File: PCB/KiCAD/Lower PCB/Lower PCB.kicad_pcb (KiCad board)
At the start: 2 copper layers, 179.5 x 163.2 mm, 0 parts

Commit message: Start of PCBs
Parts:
- added C1: 100nF, Capacitor_SMD:C_0805_2012Metric_Pad1.18x1.45mm_HandSolder, F.Cu at (-2.28, 6.00)
- added C10: 10nF, Capacitor_SMD:C_1210_3225Metric_Pad1.33x2.70mm_HandSolder, F.Cu at (-56.5, 25.0)
- added C11: 10nF, Capacitor_SMD:C_1210_3225Metric_Pad1.33x2.70mm_HandSolder, F.Cu at (-56.6, 30.5)
- added C12: 0.1uF, Capacitor_SMD:C_0805_2012Metric_Pad1.18x1.45mm_HandSolder, F.Cu at (-51.0, 31.5)
- added C13: 10nF, Capacitor_SMD:C_1210_3225Metric_Pad1.33x2.70mm_HandSolder, F.Cu at (-57.5, -30.5)
- added C14: 10nF, Capacitor_SMD:C_1210_3225Metric_Pad1.33x2.70mm_HandSolder, F.Cu at (-57.5, -24.5)
- added C15: 0.1uF, Capacitor_SMD:C_0805_2012Metric_Pad1.18x1.45mm_HandSolder, F.Cu at (-52.0, -24.0)
- added C16: 220uF, Capacitor_SMD:CP_Elec_10x10, F.Cu at (43.5, -13.0)
- added C17: 220uF, Capacitor_SMD:CP_Elec_10x10, F.Cu at (43.0, 12.5)
- added C18: 0.1uF, Capacitor_SMD:C_0805_2012Metric_Pad1.18x1.45mm_HandSolder, F.Cu at (53.0, -27.5)
- added C19: 0.1uF, Capacitor_SMD:C_0805_2012Metric_Pad1.18x1.45mm_HandSolder, F.Cu at (53.5, 27.0)
- added C2: 100nF, Capacitor_SMD:C_0805_2012Metric_Pad1.18x1.45mm_HandSolder, F.Cu at (-2.28, 9.01)
- added C20: 10nF, Capacitor_SMD:C_1210_3225Metric_Pad1.33x2.70mm_HandSolder, F.Cu at (47.5, -30.5)
- added C21: 100nF, Capacitor_SMD:C_0805_2012Metric_Pad1.18x1.45mm_HandSolder, F.Cu at (20.5, -30.0)
- added C22: 100nF, Capacitor_SMD:C_0805_2012Metric_Pad1.18x1.45mm_HandSolder, F.Cu at (20.6, -26.5)
- added C23: 22pF, Capacitor_SMD:C_0805_2012Metric_Pad1.18x1.45mm_HandSolder, F.Cu at (26.1, -30.0)
- added C24: 22pF, Capacitor_SMD:C_0805_2012Metric_Pad1.18x1.45mm_HandSolder, F.Cu at (26.1, -26.5)
- added C25: 100nF, Capacitor_SMD:C_0805_2012Metric_Pad1.18x1.45mm_HandSolder, F.Cu at (20.6, -23.0)
- added C26: 10nF, Capacitor_SMD:C_1210_3225Metric_Pad1.33x2.70mm_HandSolder, F.Cu at (47.5, -24.5)
- added C27: 0.1uF, Capacitor_SMD:C_0805_2012Metric_Pad1.18x1.45mm_HandSolder, F.Cu at (53.0, -24.0)
- added C28: 10nF, Capacitor_SMD:C_1210_3225Metric_Pad1.33x2.70mm_HandSolder, F.Cu at (48.0, 24.0)
- added C29: 10nF, Capacitor_SMD:C_1210_3225Metric_Pad1.33x2.70mm_HandSolder, F.Cu at (48.0, 30.0)
- added C3: 100nF, Capacitor_SMD:C_0805_2012Metric_Pad1.18x1.45mm_HandSolder, F.Cu at (-2.28, 12.0)
- added C30: 0.1uF, Capacitor_SMD:C_0805_2012Metric_Pad1.18x1.45mm_HandSolder, F.Cu at (53.5, 30.5)
- added C4: 22pF, Capacitor_SMD:C_0805_2012Metric_Pad1.18x1.45mm_HandSolder, F.Cu at (-2.28, 15.0)
- added C5: 22pF, Capacitor_SMD:C_0805_2012Metric_Pad1.18x1.45mm_HandSolder, F.Cu at (-2.28, 18.0)
- added C6: 220uF, Capacitor_SMD:CP_Elec_10x10, F.Cu at (-42.5, 12.5)
- added C7: 220uF, Capacitor_SMD:CP_Elec_10x10, F.Cu at (-42.0, -12.0)
- added C8: 0.1uF, Capacitor_SMD:C_0805_2012Metric_Pad1.18x1.45mm_HandSolder, F.Cu at (-51.0, 28.0)
- added C9: 0.1uF, Capacitor_SMD:C_0805_2012Metric_Pad1.18x1.45mm_HandSolder, F.Cu at (-52.0, -27.5)
- added D1: RED_LED, LED_SMD:LED_0805_2012Metric_Pad1.15x1.40mm_HandSolder, F.Cu at (2.54, 6.01)
- added D2: GREEN_LED, LED_SMD:LED_0805_2012Metric_Pad1.15x1.40mm_HandSolder, F.Cu at (2.54, 9.05)
- added D3: RED_LED, LED_SMD:LED_0805_2012Metric_Pad1.15x1.40mm_HandSolder, F.Cu at (31.0, -23.5)
- added D4: GREEN_LED, LED_SMD:LED_0805_2012Metric_Pad1.15x1.40mm_HandSolder, F.Cu at (31.0, -20.5)
- added F1: Fuse, Fuse:Fuseholder_Blade_Mini_Keystone_3568, F.Cu at (-6.20, -56.0)
- added J2: Conn_01x02, Connector_AMASS:AMASS_XT60-M_1x02_P7.20mm_Vertical, F.Cu at (-13.5, -64.6)
- added M1: Conn_01x02_Pin, Connector_Molex:Molex_KK-254_AE-6410-02A_1x02_P2.54mm_Vertical, F.Cu at (-46.5, 27.0)
- added M2: Conn_01x02_Pin, Connector_Molex:Molex_KK-254_AE-6410-02A_1x02_P2.54mm_Vertical, F.Cu at (-47.5, -28.5)
- added M3: Conn_01x02_Pin, Connector_Molex:Molex_KK-254_AE-6410-02A_1x02_P2.54mm_Vertical, F.Cu at (57.5, -28.5)
- added M4: Conn_01x02_Pin, Connector_Molex:Molex_KK-254_AE-6410-02A_1x02_P2.54mm_Vertical, F.Cu at (58.0, 26.0)
- added R1: 2.7k, Resistor_SMD:R_0805_2012Metric_Pad1.20x1.40mm_HandSolder, F.Cu at (-51.1, 24.5)
- added R12: 2.7k, Resistor_SMD:R_0805_2012Metric_Pad1.20x1.40mm_HandSolder, F.Cu at (53.0, -31.0)
- added R13: 2.7k, Resistor_SMD:R_0805_2012Metric_Pad1.20x1.40mm_HandSolder, F.Cu at (53.5, 23.5)
- added R2: 330, Resistor_SMD:R_0805_2012Metric_Pad1.20x1.40mm_HandSolder, F.Cu at (2.50, 12.1)
- added R3: 330, Resistor_SMD:R_0805_2012Metric_Pad1.20x1.40mm_HandSolder, F.Cu at (2.50, 15.0)
- added R4: 330, Resistor_SMD:R_0805_2012Metric_Pad1.20x1.40mm_HandSolder, F.Cu at (2.69, 18.1)
- added R5: 2.7k, Resistor_SMD:R_0805_2012Metric_Pad1.20x1.40mm_HandSolder, F.Cu at (-52.0, -31.0)
- added R6: 330, Resistor_SMD:R_0805_2012Metric_Pad1.20x1.40mm_HandSolder, F.Cu at (14.6, -30.0)
- added R7: 330, Resistor_SMD:R_0805_2012Metric_Pad1.20x1.40mm_HandSolder, F.Cu at (14.6, -26.5)
- added S1: 1101M2S3CGE2, 1101M2S3CGE2:1101M2S3CGE2, F.Cu at (4.00, -64.7)
- added U1: ATmega328PB-A, Package_QFP:TQFP-32_7x7mm_P0.8mm, F.Cu at (-11.8, 12.2)
- added U2: LMD18200, Package_TO_SOT_THT:TO-220-11_P3.4x5.08mm_StaggerOdd_Lead4.58mm_Vertical, F.Cu at (-50.5, 8.42)
- added U3: LMD18200, Package_TO_SOT_THT:TO-220-11_P3.4x5.08mm_StaggerOdd_Lead4.58mm_Vertical, F.Cu at (-67.4, -7.92)
- added U4: LMD18200, Package_TO_SOT_THT:TO-220-11_P3.4x5.08mm_StaggerOdd_Lead4.58mm_Vertical, F.Cu at (51.7, -8.42)
- added U5: LMD18200, Package_TO_SOT_THT:TO-220-11_P3.4x5.08mm_StaggerOdd_Lead4.58mm_Vertical, F.Cu at (68.5, 8.42)
- added U6: ATmega328PB-A, Package_QFP:TQFP-32_7x7mm_P0.8mm, F.Cu at (7.50, -8.50)
- added U7: ~, Pololu:D36V28F5, F.Cu at (0.00, -42.5)
- added Y1: Crystal, Crystal:Crystal_SMD_3225-4Pin_3.2x2.5mm_HandSoldering, F.Cu at (-13.0, 1.00)
- added Y2: Crystal, Crystal:Crystal_SMD_3225-4Pin_3.2x2.5mm_HandSoldering, F.Cu at (32.1, -28.6)
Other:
- outline, holes or cut-outs redrawn

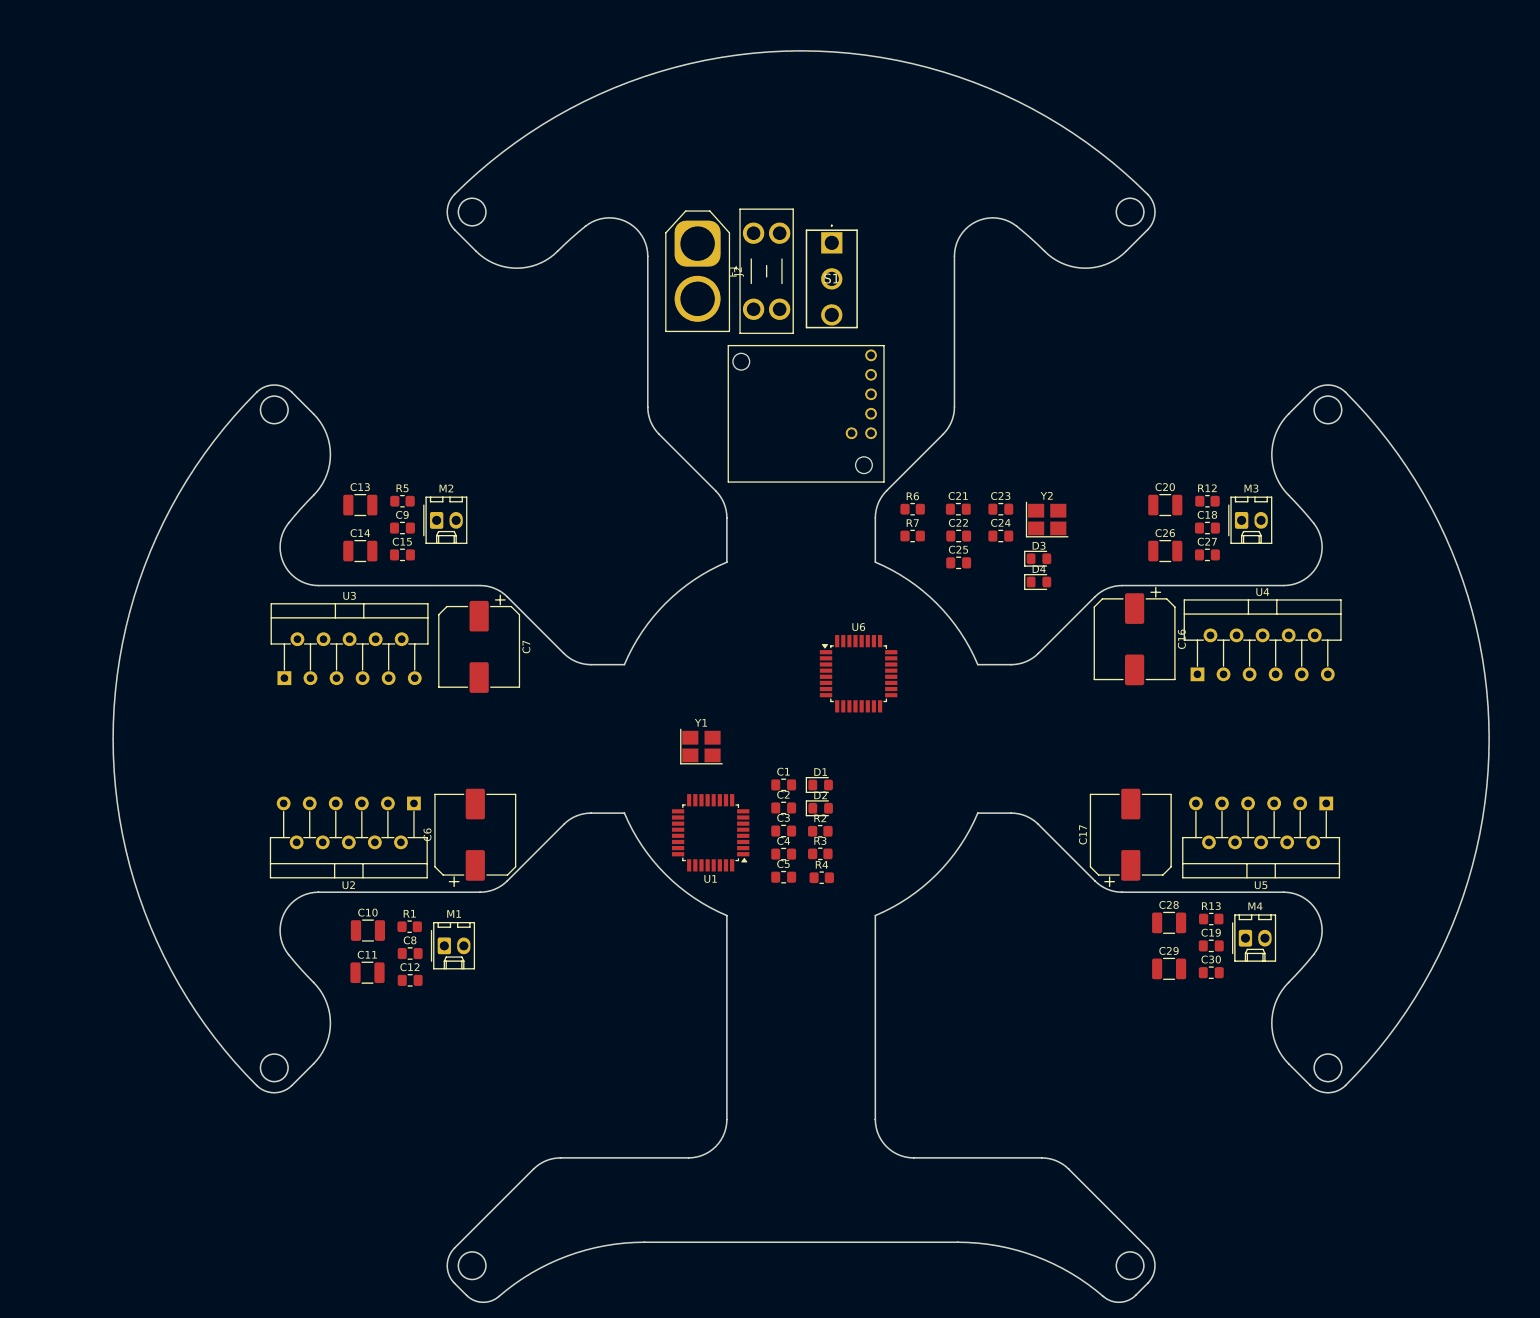
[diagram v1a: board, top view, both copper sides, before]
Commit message: Placed components on Lower PCB
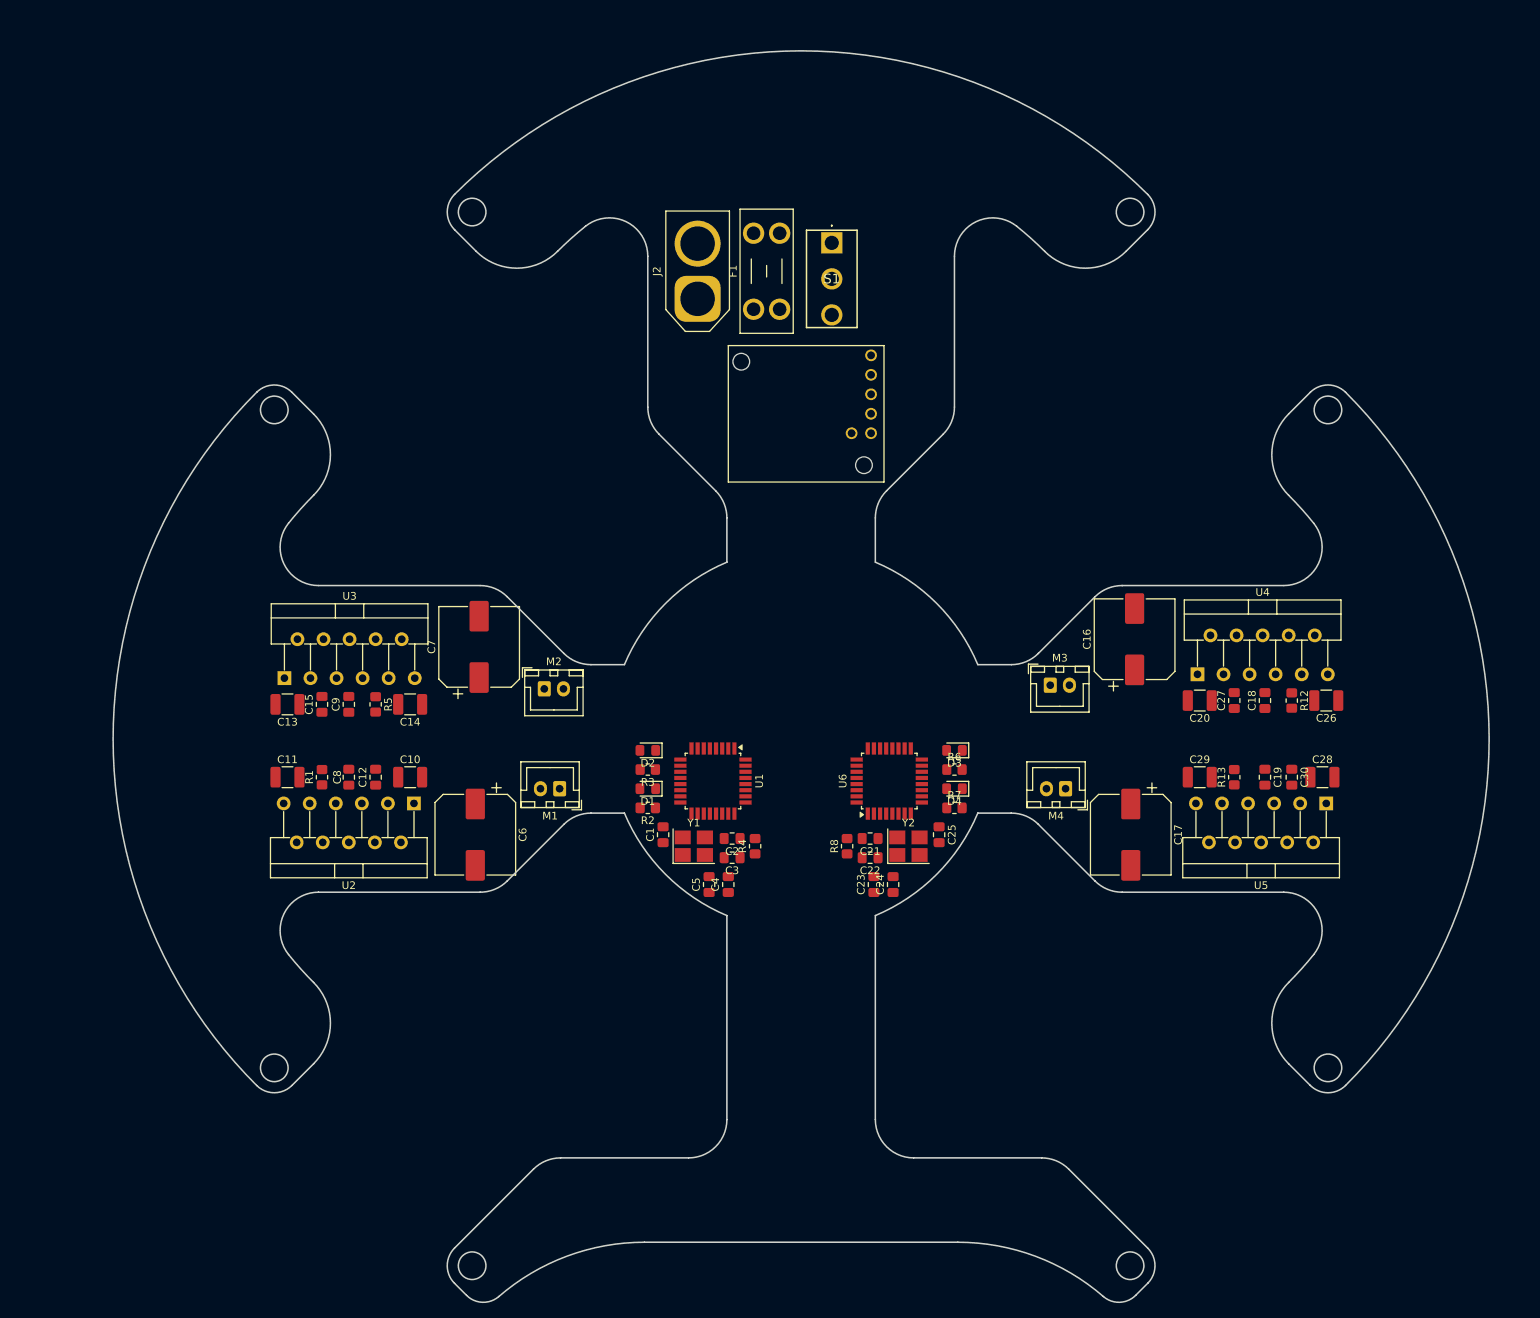
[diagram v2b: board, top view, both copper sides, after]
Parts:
- added R8: 10k, Resistor_SMD:R_0805_2012Metric_Pad1.20x1.40mm_HandSolder, F.Cu at (6.00, 14.0)
- M1, M2, M3, M4: footprint Connector_Molex:Molex_KK-254_AE-6410-02A_1x02_P2.54mm_Vertical -> Connector_JST:JST_XH_B2B-XH-A_1x02_P2.50mm_Vertical
- R4: value 330 -> 10k
- moved C23 51.7 mm to (9.50, 19.0), turned to 90 degrees
- moved C24 47.6 mm to (12.0, 19.0), turned to 90 degrees
- moved Y2 46.3 mm to (14.0, 14.0)
- moved C21 44.5 mm to (9.00, 13.0), turned to 180 degrees
- moved C22 43.5 mm to (9.00, 15.5), turned to 180 degrees
- moved R7 35.9 mm to (20.0, 9.00)
- moved C25 35.6 mm to (18.0, 12.5), turned to -90 degrees
- moved R6 34.4 mm to (20.0, 4.00)
- moved M3 32.9 mm to (32.5, -7.00)
- moved M4 30.5 mm to (34.5, 6.50), turned to 180 degrees
- moved D4 29.1 mm to (20.0, 6.50), turned to 180 degrees
- moved C26 28.7 mm to (68.5, -5.00), turned to 180 degrees
- moved R12 28.2 mm to (64.0, -5.00), turned to -90 degrees
- moved C13 27.7 mm to (-67.0, -4.50), turned to 180 degrees
- moved C28 27.6 mm to (68.0, 5.00)
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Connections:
- U6 pad 29: unconnected-(U6-~{RESET}/PC6-Pad29) -> Net-(U6-~{RESET}/PC6)

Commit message: More work to the lower PCB
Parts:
- added C31: 100nF, Capacitor_SMD:C_0805_2012Metric_Pad1.18x1.45mm_HandSolder, F.Cu at (0.00, 12.0)
- added C32: 100nF, Capacitor_SMD:C_0805_2012Metric_Pad1.18x1.45mm_HandSolder, F.Cu at (-6.50, -5.50)
- added D10: LED, LED_SMD:LED_PLCC-2_3.4x3.0mm_KA, B.Cu at (-68.4, -36.0)
- added D11: LED, LED_SMD:LED_PLCC-2_3.4x3.0mm_KA, B.Cu at (-78.1, -19.2)
- added D12: LED, LED_SMD:LED_PLCC-2_3.4x3.0mm_KA, B.Cu at (-81.5, 0.00)
- added D13: LED, LED_SMD:LED_PLCC-2_3.4x3.0mm_KA, B.Cu at (-78.1, 19.2)
- added D14: LED, LED_SMD:LED_PLCC-2_3.4x3.0mm_KA, B.Cu at (-68.4, 36.0)
- added D15: LED, LED_SMD:LED_PLCC-2_3.4x3.0mm_KA, B.Cu at (-36.0, -68.4)
- added D16: LED, LED_SMD:LED_PLCC-2_3.4x3.0mm_KA, B.Cu at (-19.2, -78.1)
- added D17: LED, LED_SMD:LED_PLCC-2_3.4x3.0mm_KA, B.Cu at (0.00, -81.5)
- added D18: LED, LED_SMD:LED_PLCC-2_3.4x3.0mm_KA, B.Cu at (19.2, -78.1)
- added D19: LED, LED_SMD:LED_PLCC-2_3.4x3.0mm_KA, B.Cu at (36.0, -68.5)
- added D20: LED, LED_SMD:LED_PLCC-2_3.4x3.0mm_KA, B.Cu at (68.4, -36.0)
- added D21: LED, LED_SMD:LED_PLCC-2_3.4x3.0mm_KA, B.Cu at (78.1, -19.2)
- added D22: LED, LED_SMD:LED_PLCC-2_3.4x3.0mm_KA, B.Cu at (81.5, 0.00)
- added D23: LED, LED_SMD:LED_PLCC-2_3.4x3.0mm_KA, B.Cu at (78.1, 19.2)
- added D24: LED, LED_SMD:LED_PLCC-2_3.4x3.0mm_KA, B.Cu at (68.4, 36.0)
- added D5: LED, LED_SMD:LED_PLCC-2_3.4x3.0mm_KA, B.Cu at (30.0, 58.0)
- added D6: LED, LED_SMD:LED_PLCC-2_3.4x3.0mm_KA, B.Cu at (0.00, 58.0)
- added D7: LED, LED_SMD:LED_PLCC-2_3.4x3.0mm_KA, B.Cu at (-15.0, 58.0)
- added D8: LED, LED_SMD:LED_PLCC-2_3.4x3.0mm_KA, B.Cu at (-30.0, 58.0)
- added D9: LED, LED_SMD:LED_PLCC-2_3.4x3.0mm_KA, B.Cu at (15.0, 58.0)
- added IC1: ADG608BRZ, ADG608BRZ:SOIC127P600X175-16N, F.Cu at (0.00, -5.50)
- added IC2: ADG608BRZ, ADG608BRZ:SOIC127P600X175-16N, F.Cu at (0.00, 5.50)
- added Q1: SFH320, LED_SMD:LED_PLCC-2_3.4x3.0mm_KA, B.Cu at (22.5, 58.0)
- added Q10: SFH320, LED_SMD:LED_PLCC-2_3.4x3.0mm_KA, B.Cu at (-9.72, -80.6)
- added Q11: SFH320, LED_SMD:LED_PLCC-2_3.4x3.0mm_KA, B.Cu at (9.72, -80.6)
- added Q12: SFH320, LED_SMD:LED_PLCC-2_3.4x3.0mm_KA, B.Cu at (28.0, -74.0)
- added Q13: SFH320, LED_SMD:LED_PLCC-2_3.4x3.0mm_KA, B.Cu at (74.0, -28.0)
- added Q14: SFH320, LED_SMD:LED_PLCC-2_3.4x3.0mm_KA, B.Cu at (80.6, -9.72)
- added Q15: SFH320, LED_SMD:LED_PLCC-2_3.4x3.0mm_KA, B.Cu at (80.6, 9.72)
- added Q16: SFH320, LED_SMD:LED_PLCC-2_3.4x3.0mm_KA, B.Cu at (74.0, 28.0)
- added Q2: SFH320, LED_SMD:LED_PLCC-2_3.4x3.0mm_KA, B.Cu at (7.50, 58.0)
- added Q3: SFH320, LED_SMD:LED_PLCC-2_3.4x3.0mm_KA, B.Cu at (-7.50, 58.0)
- added Q4: SFH320, LED_SMD:LED_PLCC-2_3.4x3.0mm_KA, B.Cu at (-22.5, 58.0)
- added Q5: SFH320, LED_SMD:LED_PLCC-2_3.4x3.0mm_KA, B.Cu at (-74.0, 28.0)
- added Q6: SFH320, LED_SMD:LED_PLCC-2_3.4x3.0mm_KA, B.Cu at (-80.6, 9.72)
- added Q7: SFH320, LED_SMD:LED_PLCC-2_3.4x3.0mm_KA, B.Cu at (-80.6, -9.72)
- added Q8: SFH320, LED_SMD:LED_PLCC-2_3.4x3.0mm_KA, B.Cu at (-74.0, -28.0)
- added Q9: SFH320, LED_SMD:LED_PLCC-2_3.4x3.0mm_KA, B.Cu at (-28.0, -74.0)
- added R10: 10k, Resistor_SMD:R_0805_2012Metric_Pad1.20x1.40mm_HandSolder, F.Cu at (6.00, 46.0)
- added R11: 330, Resistor_SMD:R_0805_2012Metric_Pad1.20x1.40mm_HandSolder, F.Cu at (0.00, 50.5)
- added R14: 10k, Resistor_SMD:R_0805_2012Metric_Pad1.20x1.40mm_HandSolder, F.Cu at (2.00, 46.0)
- added R15: 330, Resistor_SMD:R_0805_2012Metric_Pad1.20x1.40mm_HandSolder, F.Cu at (-3.50, 50.5)
- added R16: 10k, Resistor_SMD:R_0805_2012Metric_Pad1.20x1.40mm_HandSolder, F.Cu at (-2.00, 46.0)
- added R17: 330, Resistor_SMD:R_0805_2012Metric_Pad1.20x1.40mm_HandSolder, F.Cu at (-7.00, 50.5)
- added R18: 10k, Resistor_SMD:R_0805_2012Metric_Pad1.20x1.40mm_HandSolder, F.Cu at (-6.00, 46.0)
- added R19: 330, Resistor_SMD:R_0805_2012Metric_Pad1.20x1.40mm_HandSolder, F.Cu at (3.50, 50.5)
- added R20: 330, Resistor_SMD:R_0805_2012Metric_Pad1.20x1.40mm_HandSolder, F.Cu at (-74.0, -10.0)
- added R21: 330, Resistor_SMD:R_0805_2012Metric_Pad1.20x1.40mm_HandSolder, F.Cu at (-74.0, -5.00)
- added R22: 330, Resistor_SMD:R_0805_2012Metric_Pad1.20x1.40mm_HandSolder, F.Cu at (-74.0, 0.00)
- added R23: 330, Resistor_SMD:R_0805_2012Metric_Pad1.20x1.40mm_HandSolder, F.Cu at (-74.0, 5.00)
- added R24: 330, Resistor_SMD:R_0805_2012Metric_Pad1.20x1.40mm_HandSolder, F.Cu at (-74.0, 10.0)
- added R25: 330, Resistor_SMD:R_0805_2012Metric_Pad1.20x1.40mm_HandSolder, F.Cu at (-10.5, -75.0)
- added R26: 330, Resistor_SMD:R_0805_2012Metric_Pad1.20x1.40mm_HandSolder, F.Cu at (-5.50, -75.0)
- added R27: 330, Resistor_SMD:R_0805_2012Metric_Pad1.20x1.40mm_HandSolder, F.Cu at (-0.48, -75.0)
- added R28: 330, Resistor_SMD:R_0805_2012Metric_Pad1.20x1.40mm_HandSolder, F.Cu at (4.50, -75.0)
- added R29: 330, Resistor_SMD:R_0805_2012Metric_Pad1.20x1.40mm_HandSolder, F.Cu at (9.50, -75.0)
- added R30: 330, Resistor_SMD:R_0805_2012Metric_Pad1.20x1.40mm_HandSolder, F.Cu at (75.0, -10.0)
- added R31: 330, Resistor_SMD:R_0805_2012Metric_Pad1.20x1.40mm_HandSolder, F.Cu at (75.0, -5.00)
- added R32: 330, Resistor_SMD:R_0805_2012Metric_Pad1.20x1.40mm_HandSolder, F.Cu at (75.0, 0.00)
- added R33: 330, Resistor_SMD:R_0805_2012Metric_Pad1.20x1.40mm_HandSolder, F.Cu at (75.0, 5.00)
- added R34: 330, Resistor_SMD:R_0805_2012Metric_Pad1.20x1.40mm_HandSolder, F.Cu at (75.0, 10.0)
- added R35: 10k, Resistor_SMD:R_0805_2012Metric_Pad1.20x1.40mm_HandSolder, F.Cu at (-74.0, 7.50)
- added R36: 10k, Resistor_SMD:R_0805_2012Metric_Pad1.20x1.40mm_HandSolder, F.Cu at (-74.0, 2.50)
- added R37: 10k, Resistor_SMD:R_0805_2012Metric_Pad1.20x1.40mm_HandSolder, F.Cu at (-74.0, -2.50)
- added R38: 10k, Resistor_SMD:R_0805_2012Metric_Pad1.20x1.40mm_HandSolder, F.Cu at (-74.0, -7.50)
- added R39: 10k, Resistor_SMD:R_0805_2012Metric_Pad1.20x1.40mm_HandSolder, F.Cu at (-8.00, -75.0)
- added R40: 10k, Resistor_SMD:R_0805_2012Metric_Pad1.20x1.40mm_HandSolder, F.Cu at (-3.00, -75.0)
- added R41: 10k, Resistor_SMD:R_0805_2012Metric_Pad1.20x1.40mm_HandSolder, F.Cu at (2.00, -75.0)
- added R42: 10k, Resistor_SMD:R_0805_2012Metric_Pad1.20x1.40mm_HandSolder, F.Cu at (7.00, -75.0)
- added R43: 10k, Resistor_SMD:R_0805_2012Metric_Pad1.20x1.40mm_HandSolder, F.Cu at (75.0, -7.50)
- added R44: 10k, Resistor_SMD:R_0805_2012Metric_Pad1.20x1.40mm_HandSolder, F.Cu at (75.0, -2.50)
- added R45: 10k, Resistor_SMD:R_0805_2012Metric_Pad1.20x1.40mm_HandSolder, F.Cu at (75.0, 2.50)
- added R46: 10k, Resistor_SMD:R_0805_2012Metric_Pad1.20x1.40mm_HandSolder, F.Cu at (75.0, 7.50)
- added R9: 330, Resistor_SMD:R_0805_2012Metric_Pad1.20x1.40mm_HandSolder, F.Cu at (7.00, 50.5)
- Y1, Y2: value Crystal -> Crystal_GND24; footprint Crystal:Crystal_SMD_3225-4Pin_3.2x2.5mm_HandSoldering -> Crystal:Crystal_SMD_5032-4Pin_5.0x3.2mm
- moved F1 12.2 mm to (-4.96, -68.2), turned to 0 degrees
- moved S1 11.3 mm to (-4.70, -57.5), turned to -90 degrees
- moved C9 4.74 mm to (-63.5, -6.00), turned to -90 degrees
- moved C12 4.61 mm to (-60.0, 6.00)
- moved C18 4.12 mm to (56.5, -6.00), turned to -90 degrees
- moved C30 4.12 mm to (60.0, 6.00), turned to 90 degrees
- moved C27 3.64 mm to (60.0, -6.00), turned to -90 degrees
- moved C19 3.16 mm to (63.5, 6.00), turned to 90 degrees
- moved C15 2.92 mm to (-60.0, -6.00), turned to -90 degrees
- moved C8 2.69 mm to (-56.5, 6.00), turned to 90 degrees
- moved C13 2.24 mm to (-68.0, -6.50)
- moved C14 2.24 mm to (-52.0, -6.50)
- moved C7 2.24 mm to (-44.0, -13.0)
- moved U3 1.93 mm to (-68.5, -9.50)
- moved C10 1.80 mm to (-52.0, 6.50)
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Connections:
- Y1 pad 1: Net-(U1-XTAL2/PB7) -> Net-(U1-XTAL1/PB6)
- Y1 pad 2: Net-(U1-XTAL1/PB6) -> unconnected-(Y1-Pad2)
- Y1 pad 3: (no net) -> Net-(U1-XTAL2/PB7)
- Y1 pad 4: (no net) -> unconnected-(Y1-Pad4)
- Y2 pad 2: Net-(U6-XTAL2/PB7) -> unconnected-(Y2-Pad2)
- Y2 pad 3: (no net) -> Net-(U6-XTAL2/PB7)
- Y2 pad 4: (no net) -> unconnected-(Y2-Pad4)
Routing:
- net +12V: track 0.00 -> 221.2 mm
- net MOTOR_1_BRAKE: track 0.00 -> 197.7 mm
- net Net-(M3-Pin_1): track 0.00 -> 48.0 mm
- net Net-(M2-Pin_2): track 0.00 -> 47.9 mm
- net Net-(M4-Pin_2): track 0.00 -> 47.9 mm
- net Net-(M1-Pin_1): track 0.00 -> 47.9 mm
- net Net-(M4-Pin_1): track 0.00 -> 30.1 mm
- net Net-(M1-Pin_2): track 0.00 -> 29.8 mm
- net Net-(M3-Pin_2): track 0.00 -> 29.8 mm
- net Net-(M2-Pin_1): track 0.00 -> 29.8 mm
- net Net-(U5-CURRENT_SENSE_OUTPUT): track 0.00 -> 16.6 mm
- net Net-(S1-COM): track 0.00 -> 12.8 mm
- net Net-(J2-Pin_2): track 0.00 -> 12.0 mm
- net Net-(U4-CURRENT_SENSE_OUTPUT): track 0.00 -> 11.1 mm
- net Net-(U3-CURRENT_SENSE_OUTPUT): track 0.00 -> 11.1 mm
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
